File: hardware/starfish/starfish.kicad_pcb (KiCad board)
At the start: 4 copper layers, 100 x 100 mm, 260 parts, among them J1 SWD, J1001 Pump, J1101 Pump, J1201 Valve, J1301 Valve, J1401 Motor, J1501 Motor, J1601 Motor, J201 DC in, J202 DC thru, J401 Cam LED, J402 Aux out, J403 Voltage, J404 Inputs, J405 Qwiic, J406 Qwiic, J407 USB B, J801 Feeders, Q1001 PSMN011-30YLC, Q1101 PSMN011-30YLC, Q201 DMP3037LSS-13, SW301 RESET, SW302 BOOTSEL, U1201 DRV120PWR, U1301 DRV120PWR, U1401 TMC2209, U1501 TMC2209, U1601 TMC2209, U201 VX7805-500, U202 MIC5317-3.3, U301 RP2040, U302 W25Q128JVS, U401 74HC2G34, U402 74HC2G34, U403 TVS, U501 PCA9545, U601 XGZP6857D, U701 XGZP6857D, U801 MAX3078E, U901 74HC2G34, Y301 12MHz

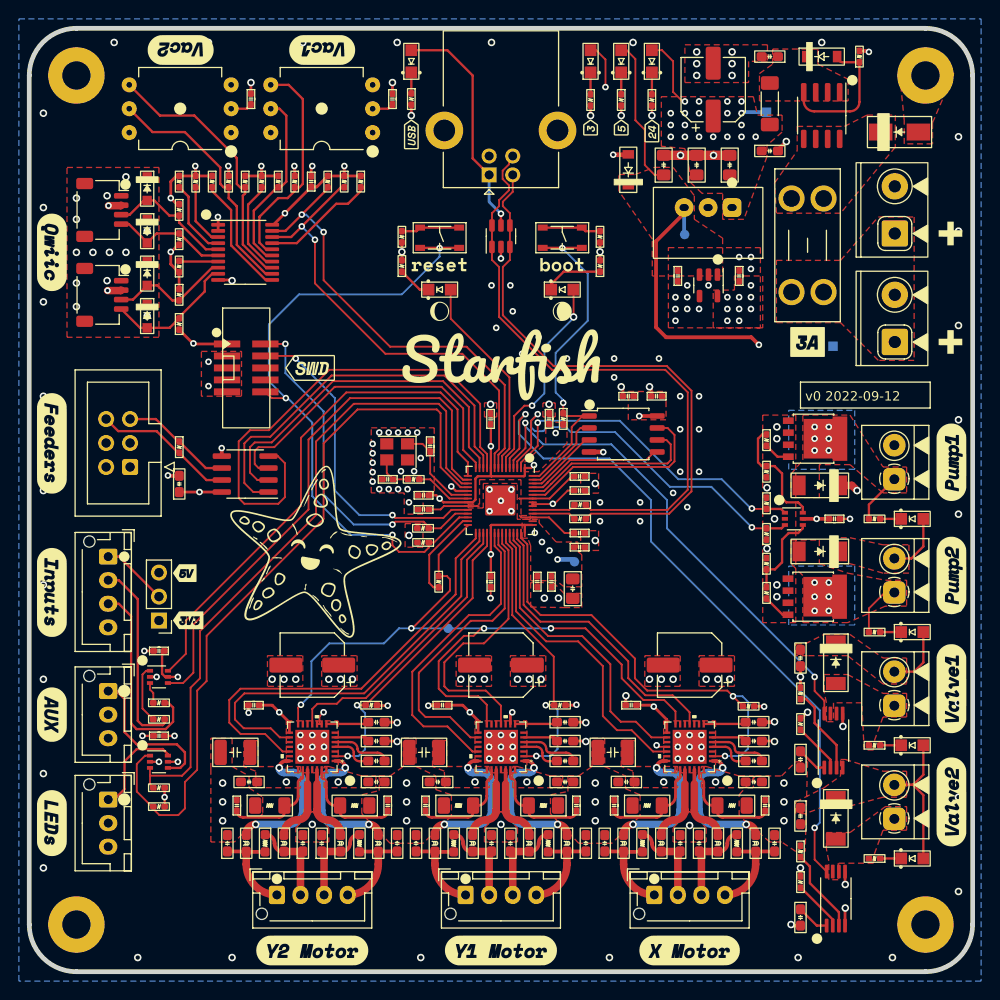
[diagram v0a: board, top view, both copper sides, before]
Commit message: Redo ground stitching
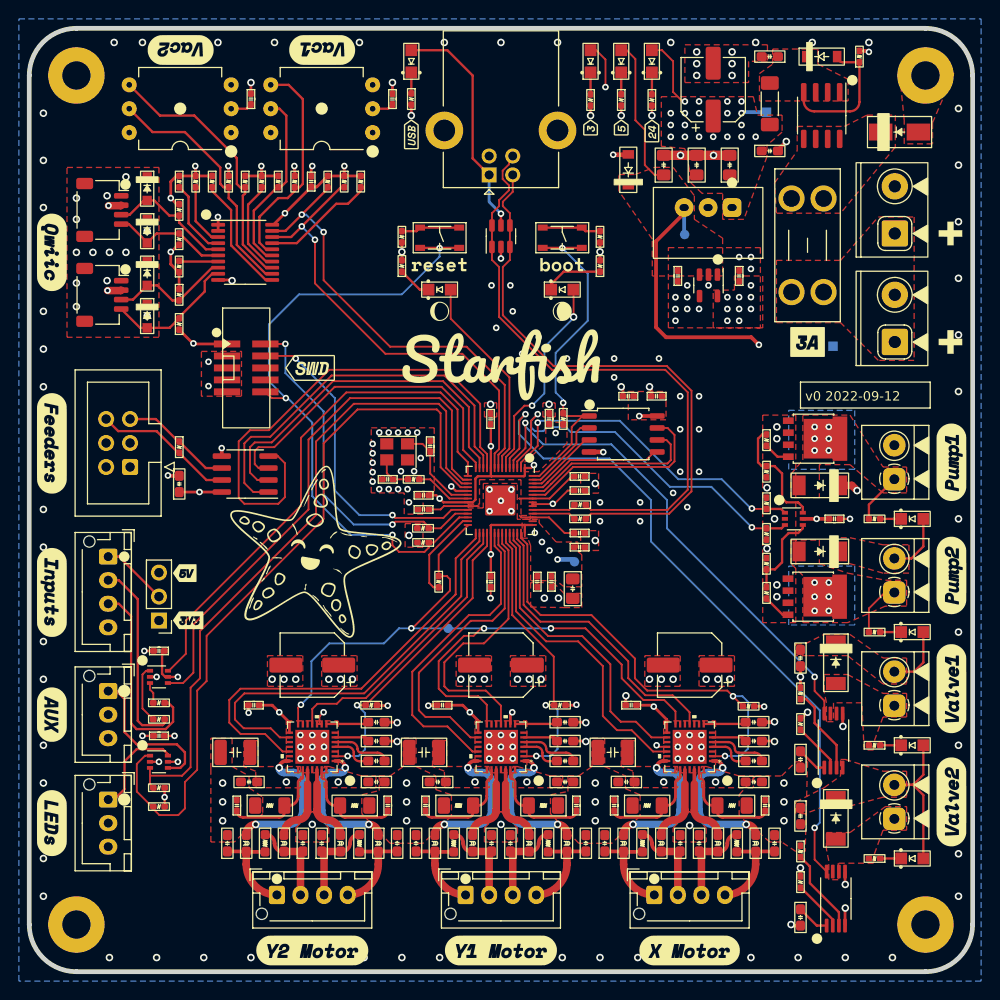
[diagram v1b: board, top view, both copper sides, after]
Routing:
- net GND: vias 215 -> 235
